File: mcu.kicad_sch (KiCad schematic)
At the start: 23 parts

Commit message: finished schematics
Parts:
- removed U?: 3k3, Resistor_SMD:R_0603_1608Metric, symbol Device:R
- U44: renamed from U?; LCSC# (none) -> C730111
- gave numbers to parts that had none: 21
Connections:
- net CAN_RX: now also U44.40 (PB3)
- net CAN_SLP: now also U44.44 (PB7)
- net CAN_TX: now also U44.41 (PB4)
- net DISP_RX: now also U44.29 (PB15)
- net DISP_TX: now also U44.22 (PB10)
- net HALL_A: now also U44.2 (PC13)
- net HALL_B: now also U44.3 (OSC32_IN/PC14)
- net HALL_C: now also U44.4 (OSC32_OUT/PC15)
- net PULSE_CRK: now also U44.13 (PA5)
- net PULSE_MOT: now also U44.18 (PB2)
- net PWM_AN: now also U44.15 (PA7); no longer U44.40 (PB3)
- net PWM_BN: now also U44.16 (PB0); no longer U44.41 (PB4)
- net PWM_BREAK: now also U44.32 (PA10); no longer U44.22 (PB10), U44.44 (PB7)
- net at U51.2: now also U44.39 (PA15)
- net at U44.11 (PA3): now also U47.2
- net at U44.12 (PA4): now also U49.2
- no-connect marks 5 -> 7
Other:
- company: Thunderdrive GmbH -> UNIMOC universal motor controller
- title: UNIMOC Hardware 4850 -> (BCC) Battery Case Controller
- moved on the sheet: U33, U35, U37, U44, U46, U47, U48, U49, U50, U51, U52, U53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

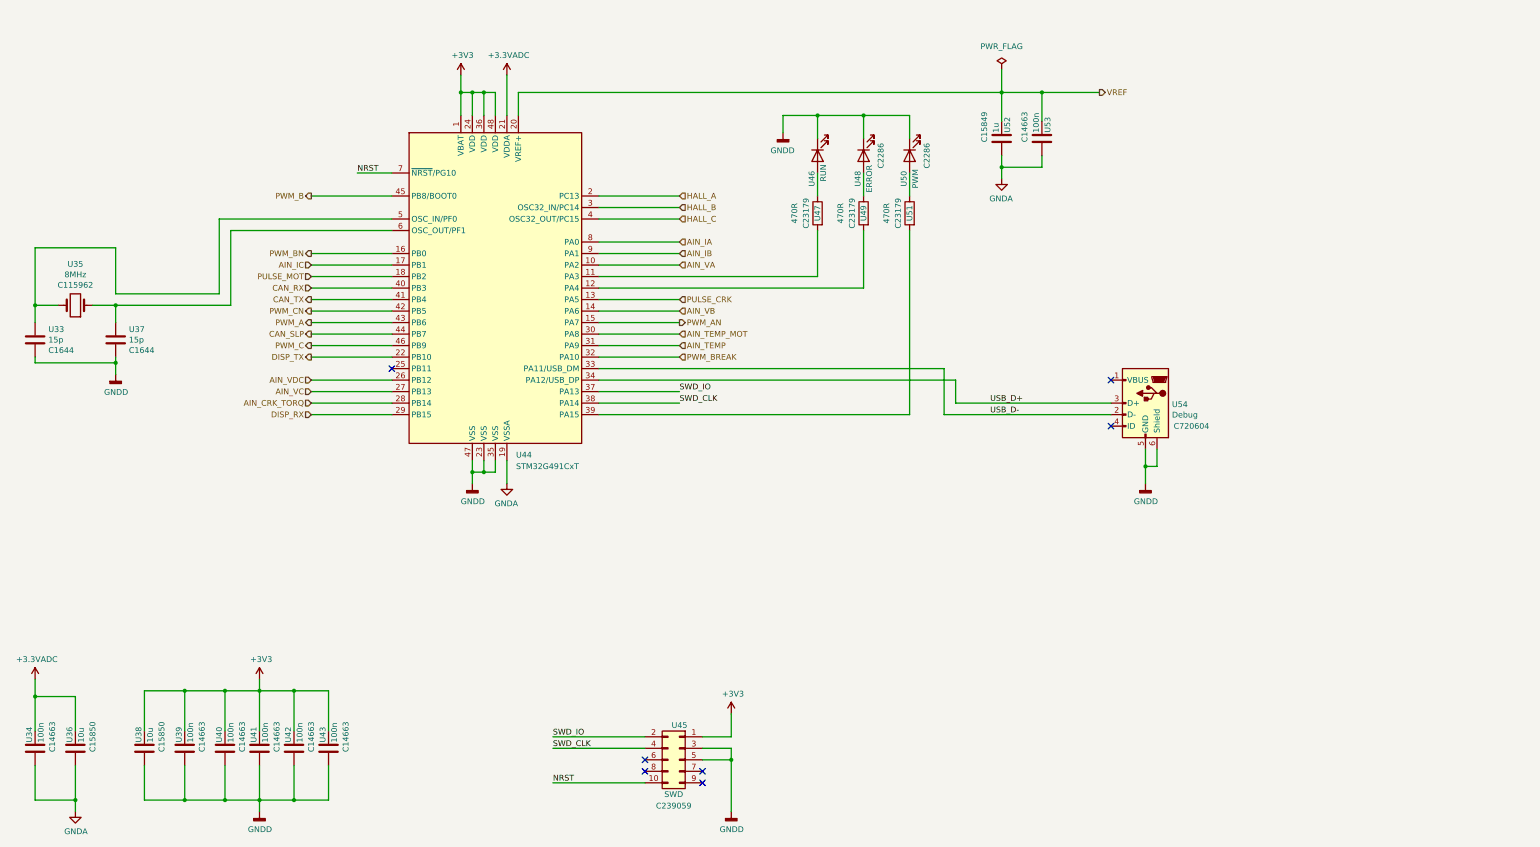
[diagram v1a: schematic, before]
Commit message: Placing first round finished
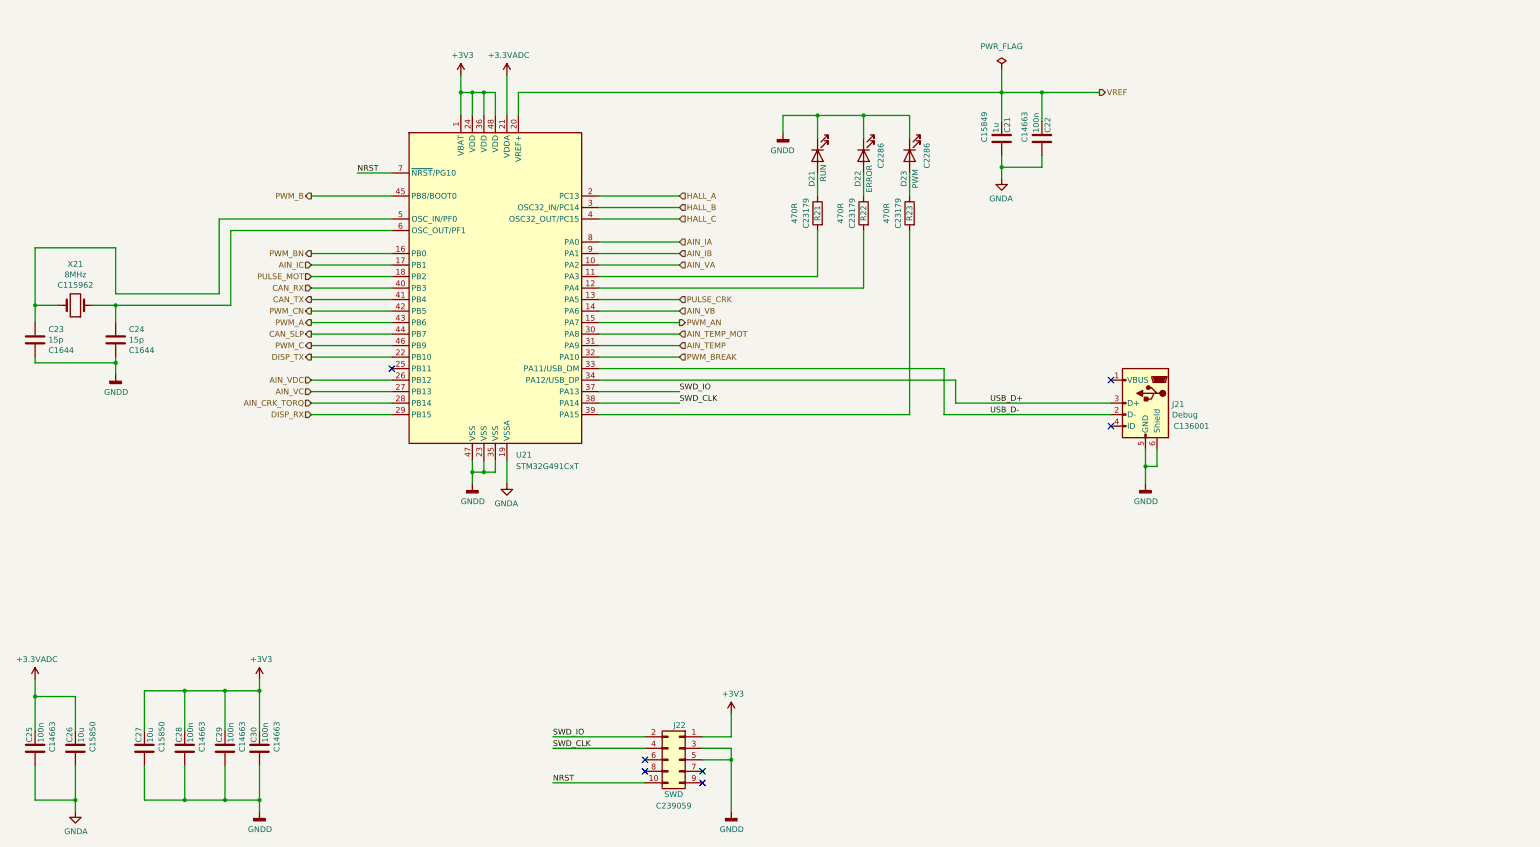
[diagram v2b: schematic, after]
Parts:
- removed U42, U43: 100n, Capacitor_SMD:C_0603_1608Metric, symbol Device:C
- J21: renamed from U54; footprint Connector_USB:USB_Micro-B_Wuerth_614105150721_Vertical -> Connector_USB:USB_Micro-AB_Molex_47590-0001; LCSC# C720604 -> C136001
- renumbered U52 to C21, U53 to C22, U33 to C23, U37 to C24, U34 to C25, U36 to C26, U38 to C27, U39 to C28, U40 to C29, U41 to C30, U46 to D21, U48 to D22, U50 to D23, U45 to J22, U47 to R21, U49 to R22, U51 to R23, U44 to U21, U35 to X21

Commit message: just the silk open
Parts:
- renumbered C21 to C89, C22 to C90, C23 to C91, C24 to C92, C25 to C93, C26 to C94, C27 to C95, C28 to C96, C29 to C97, C30 to C98, D21 to D41, D22 to D42, D23 to D43, J21 to J42, J22 to J43, R21 to R87, R22 to R88, R23 to R89, U21 to U43, X21 to X31
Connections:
- net PWM_BREAK: now also U43.25 (PB11)
- no-connect marks 7 -> 6

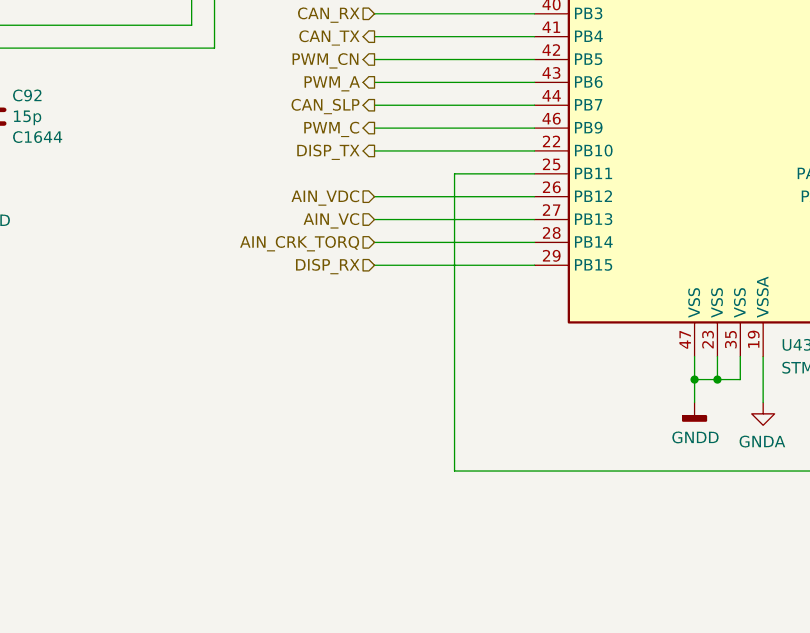
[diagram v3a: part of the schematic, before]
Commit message: Fixed pinning error for Display RX and PWM Break
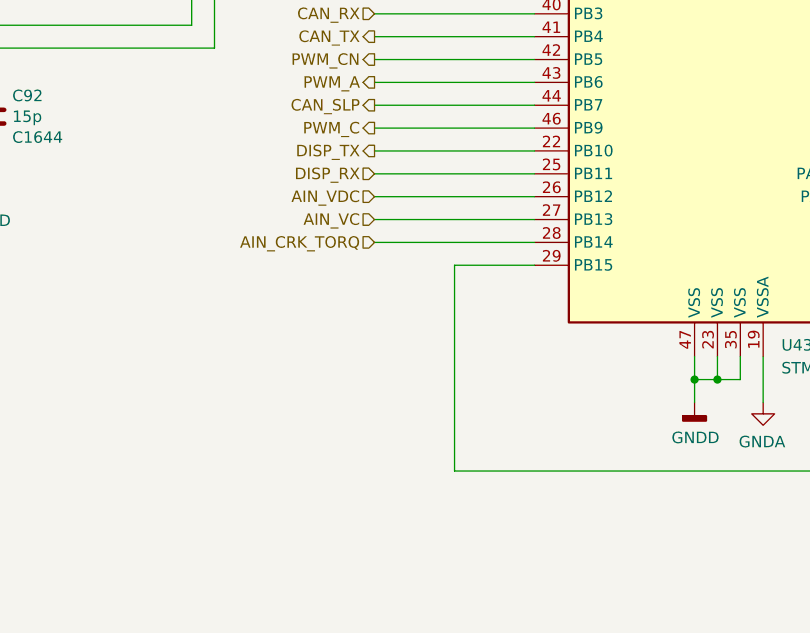
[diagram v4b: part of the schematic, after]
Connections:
- net DISP_RX: now also U43.25 (PB11); no longer U43.29 (PB15)
- net PWM_BREAK: now also U43.29 (PB15); no longer U43.25 (PB11)
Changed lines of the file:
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@@
-    (stroke (width 0) (type default) (color 0 0 0 0))
-  )
-  (wire (pts (xy 88.9 93.98) (xy 97.79 93.98))
     (stroke (width 0) (type default) (color 0 0 0 0))
   )
@@
     (stroke (width 0) (type default) (color 0 0 0 0))
   )
+  (wire (pts (xy 88.9 127) (xy 88.9 104.14))
+    (stroke (width 0) (type default) (color 0 0 0 0))
+  )
   (wire (pts (xy 52.07 181.61) (xy 52.07 189.23))
     (stroke (width 0) (type default) (color 0 0 0 0))
@@
     (stroke (width 0) (type default) (color 0 0 0 0))
   )
+  (wire (pts (xy 80.01 93.98) (xy 97.79 93.98))
+    (stroke (width 0) (type default) (color 0 0 0 0))
+  )
   (wire (pts (xy 266.7 115.57) (xy 264.16 115.57))
     (stroke (width 0) (type default) (color 0 0 0 0))
@@
     (stroke (width 0) (type default) (color 0 0 0 0))
   )
-  (wire (pts (xy 88.9 127) (xy 88.9 93.98))
-    (stroke (width 0) (type default) (color 0 0 0 0))
-  )
   (wire (pts (xy 222.25 101.6) (xy 256.54 101.6))
     (stroke (width 0) (type default) (color 0 0 0 0))
@@
     (stroke (width 0) (type default) (color 0 0 0 0))
   )
-  (wire (pts (xy 97.79 104.14) (xy 80.01 104.14))
-    (stroke (width 0) (type default) (color 0 0 0 0))
-  )
   (wire (pts (xy 97.79 101.6) (xy 80.01 101.6))
     (stroke (width 0) (type default) (color 0 0 0 0))
@@
     (stroke (width 0) (type default) (color 0 0 0 0))
   )
+  (wire (pts (xy 88.9 104.14) (xy 97.79 104.14))
+    (stroke (width 0) (type default) (color 0 0 0 0))
+  )
   (wire (pts (xy 219.71 104.14) (xy 256.54 104.14))
     (stroke (width 0) (type default) (color 0 0 0 0))
@@
     (effects (font (size 1.27 1.27)) (justify right))
   )
-  (hierarchical_label "DISP_RX" (shape input) (at 80.01 104.14 180)
-    (effects (font (size 1.27 1.27)) (justify right))
-  )
+  (hierarchical_label "DISP_RX" (shape input) (at 80.01 93.98 180)
+    (effects (font (size 1.27 1.27)) (justify right))
+  )
